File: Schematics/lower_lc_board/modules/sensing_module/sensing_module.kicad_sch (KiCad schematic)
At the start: 17 parts, among them J4 HALL-1, J5 HALL-2, U9 ADC_ADS131M04IPWR

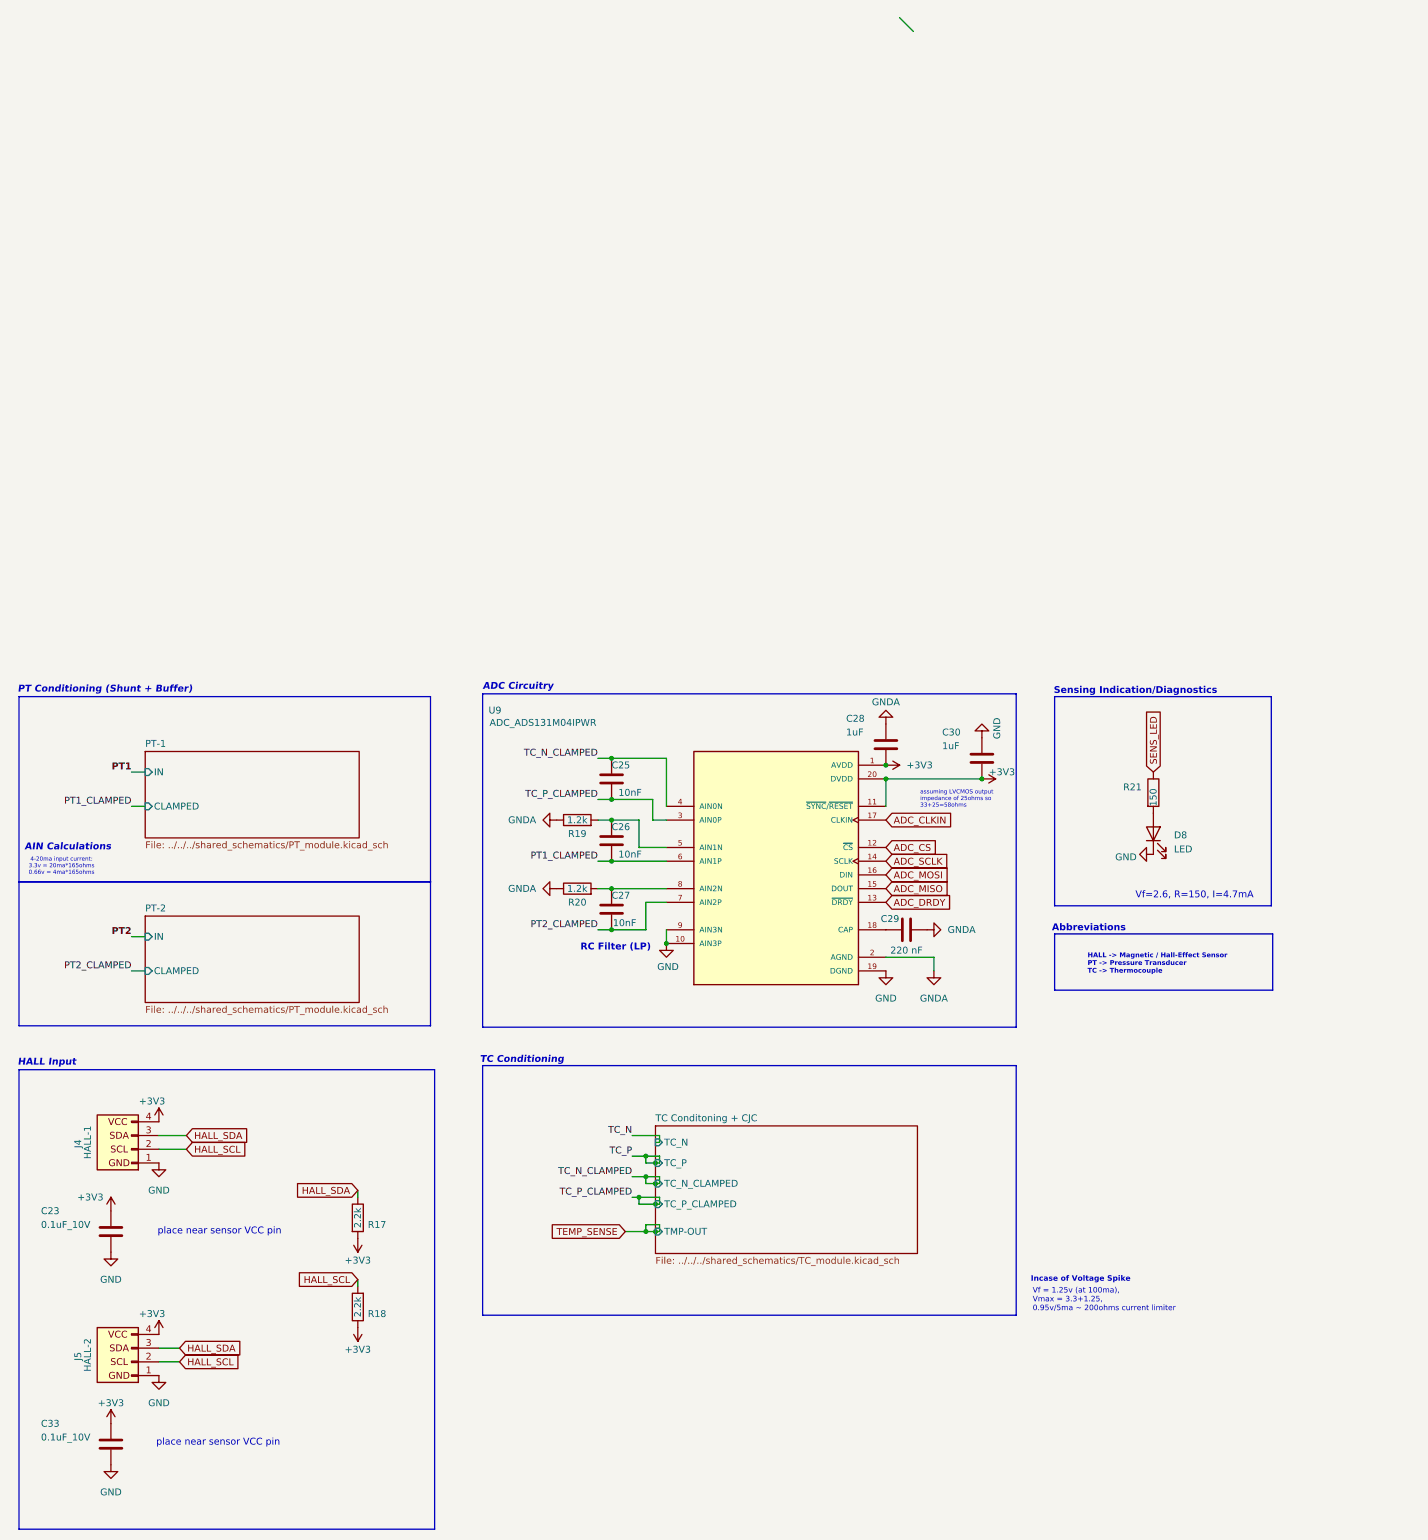
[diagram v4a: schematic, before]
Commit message: add power switching for PTs (schematic only)
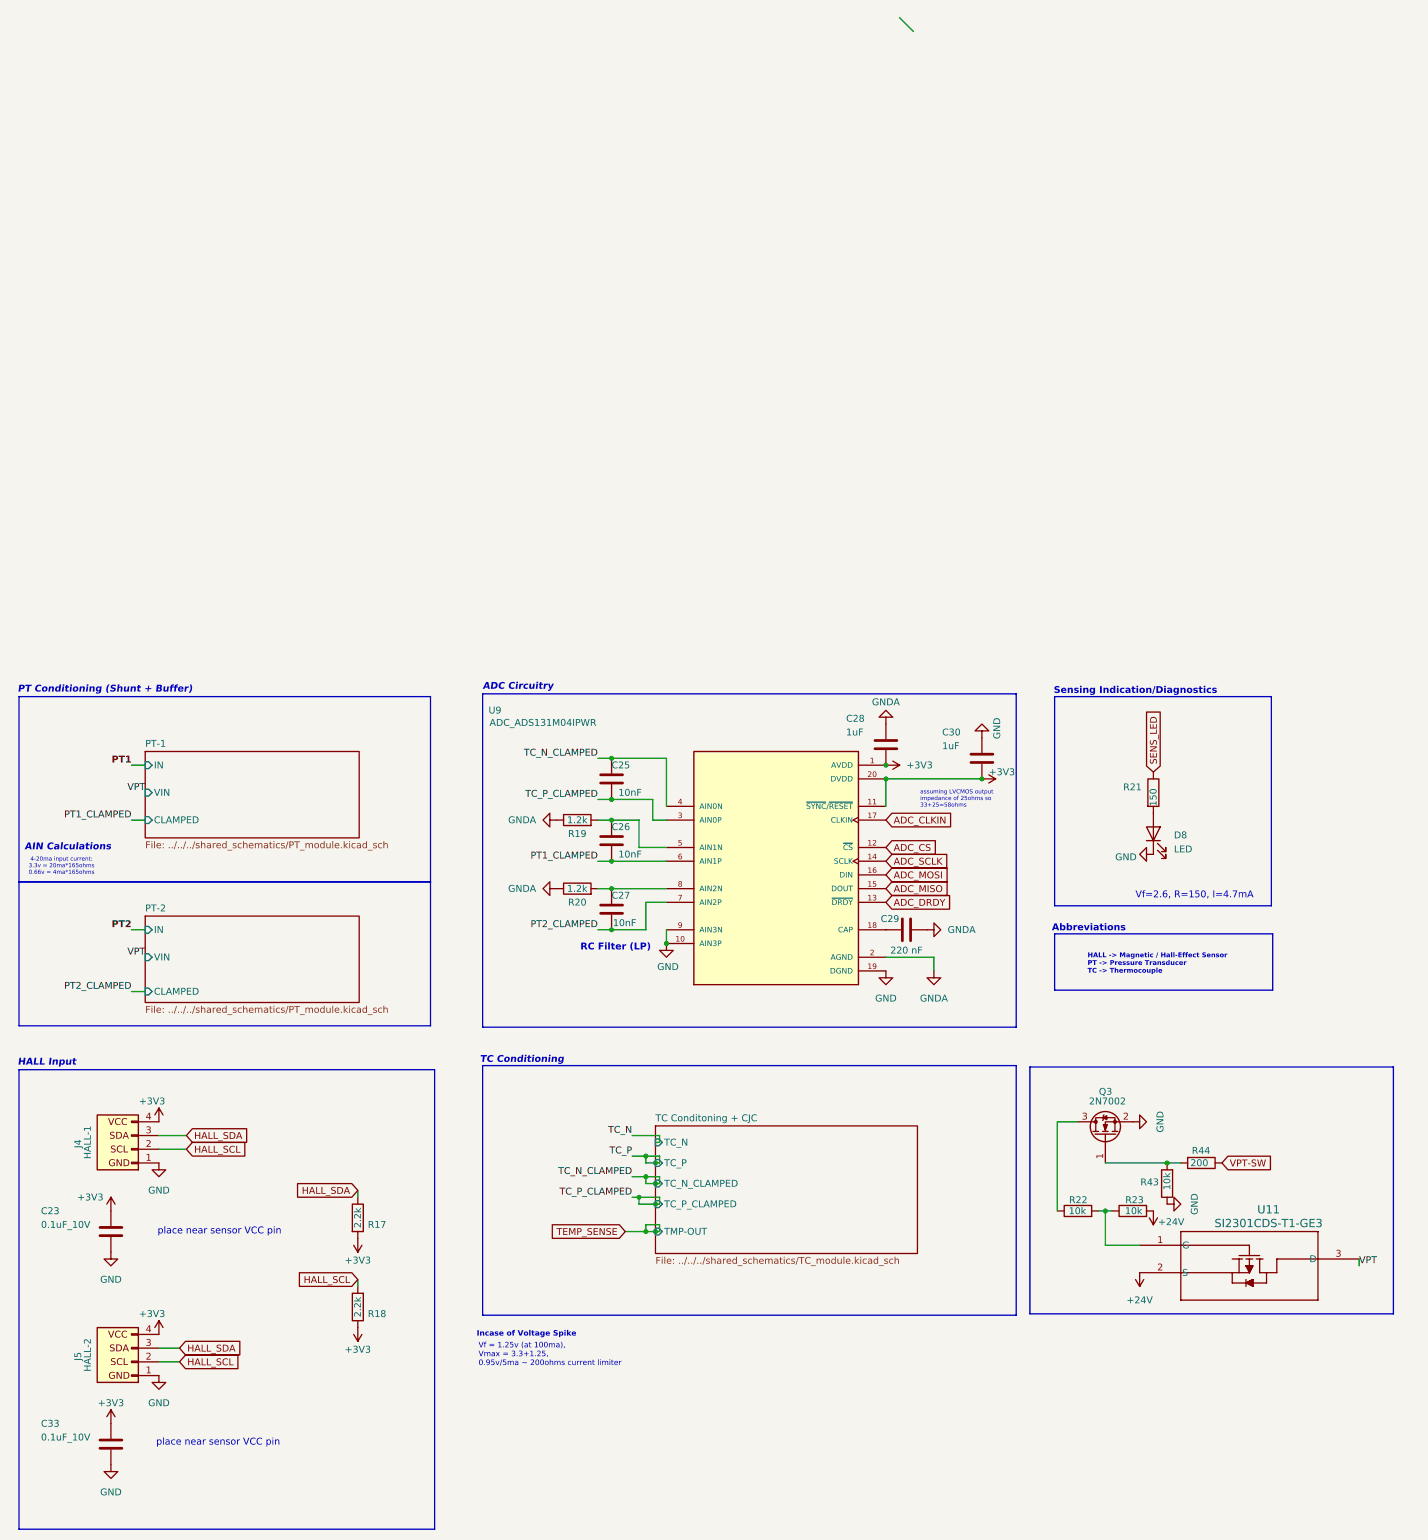
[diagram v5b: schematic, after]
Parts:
- added Q3: 2N7002, Package_TO_SOT_SMD:SOT-23, symbol Transistor_FET:2N7002
- added R22: 10k, Resistor_SMD:R_0402_1005Metric, symbol Device:R
- added R23, R43: 10k, Resistor_SMD:R_0603_1608Metric, symbol Device:R
- added R44: 200, Resistor_SMD:R_0402_1005Metric, symbol Device:R
- added U11: SI2301CDS-T1-GE3, ul_SI2301CDS-T1-GE3:TO-236_VIS, symbol SI2301:SI2301CDS-T1-GE3
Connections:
- net GND: now also Q3.2 (S), R43.1
- new net: Q3.1 (G), R43.2, R44.2
- new net: Q3.3 (D), R22.1
- new net: R22.2, R23.1, U11.1 (G)
- new net +24V: R23.2, U11.2 (S)
- new net VPT: U11.3 (D)
- new net VPT-SW: R44.1
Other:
- sheet PT-1 ports: added VIN; removed none
- sheet PT-2 ports: added VIN; removed none

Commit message: more layout work, add testing code
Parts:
- removed D8: LED, LED_SMD:LED_0603_1608Metric, symbol Device:LED
- removed R21: 150, Resistor_SMD:R_0603_1608Metric, symbol Device:R
- R23: footprint Resistor_SMD:R_0603_1608Metric -> Resistor_SMD:R_0402_1005Metric
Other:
- note removed: "Sensing Indication/Diagnostics"
- note removed: "Vf=2.6, R=150, I=4.7mA"

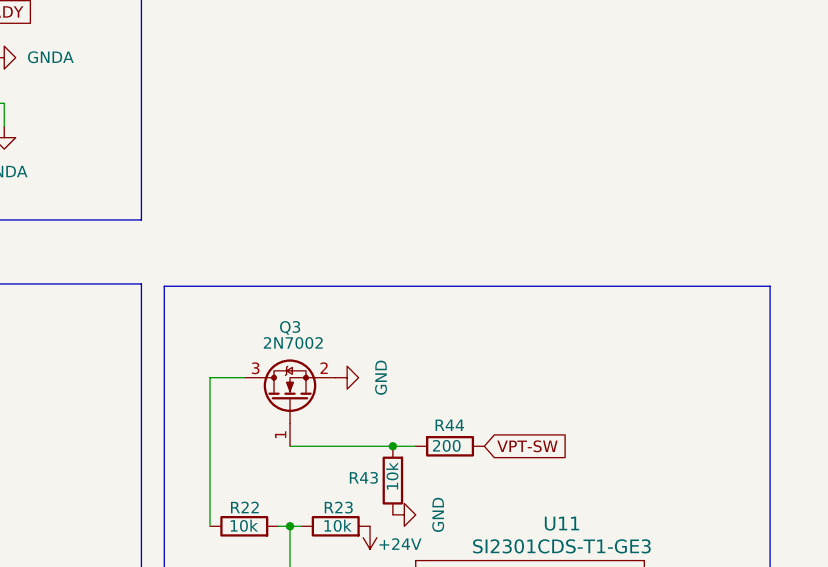
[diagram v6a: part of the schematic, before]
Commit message: add buzzer circuitry, some layout work
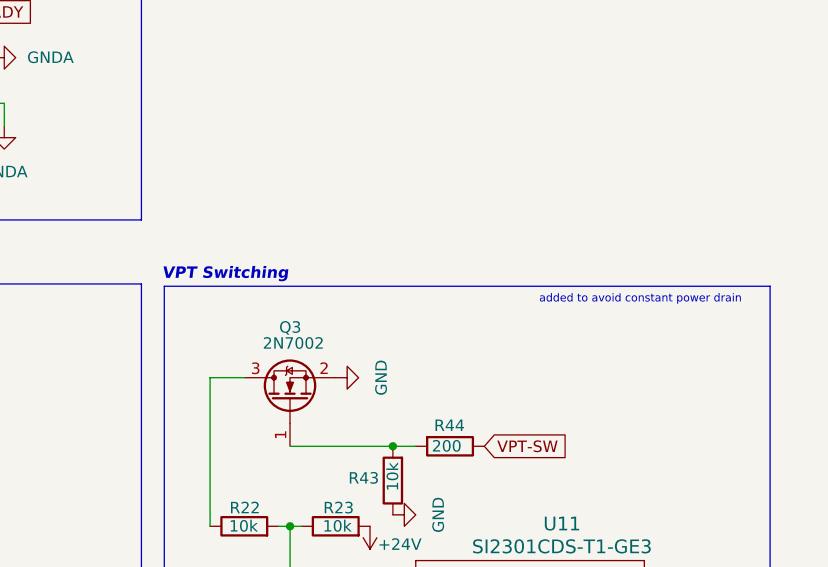
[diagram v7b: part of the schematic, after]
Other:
- note added: "VPT Switching"
- note added: "added to avoid constant power drain"
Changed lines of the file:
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@@
+		)
+	)
+	(text "VPT Switching"
+		(exclude_from_sim no)
+		(at 211.836 100.33 0)
+		(effects
+			(font
+				(size 1.27 1.27)
+				(thickness 0.254)
+				(bold yes)
+				(italic yes)
+				(color 0 0 0 1)
+			)
+			(justify left)
+		)
+	)
+	(text "added to avoid constant power drain"
+		(exclude_from_sim no)
+		(at 253.746 103.124 0)
+		(effects
+			(font
+				(size 0.889 0.889)
+				(color 0 0 0 1)
+			)
+			(justify left)
 		)
 	)
@@
 			)
 		)
-		(property "Datasheet" "https://www.onsemi.com/pub/Collateral/NDS7002A-D.PDF"
+		(property "Datasheet" "${KIPRJMOD}/../../Datasheets/NMOSFET-NDS7002A-D.PDF"
 			(at 229.87 109.22 0)
 			(effects

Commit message: organizational work
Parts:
- C23, C33: value 0.1uF_10V -> 0.1uF
- C25, C26, C27: JLCPCB (none) -> C57112
- C28, C30: JLCPCB (none) -> C15849
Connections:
- net GND: no longer U9.10 (AIN3P), U9.9 (AIN3N)
- net GNDA: now also U9.10 (AIN3P), U9.9 (AIN3N)
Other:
- moved on the sheet: C23, C25, C26, C27, C28, C29, C30, C33, J4, J5, Q3, R17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
